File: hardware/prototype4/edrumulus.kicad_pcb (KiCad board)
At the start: 2 copper layers, 67 parts, among them J1 Trigger Connector, J2 Raspberry Pi GPIO pins, U1 ESP32-DEVKIT-V1

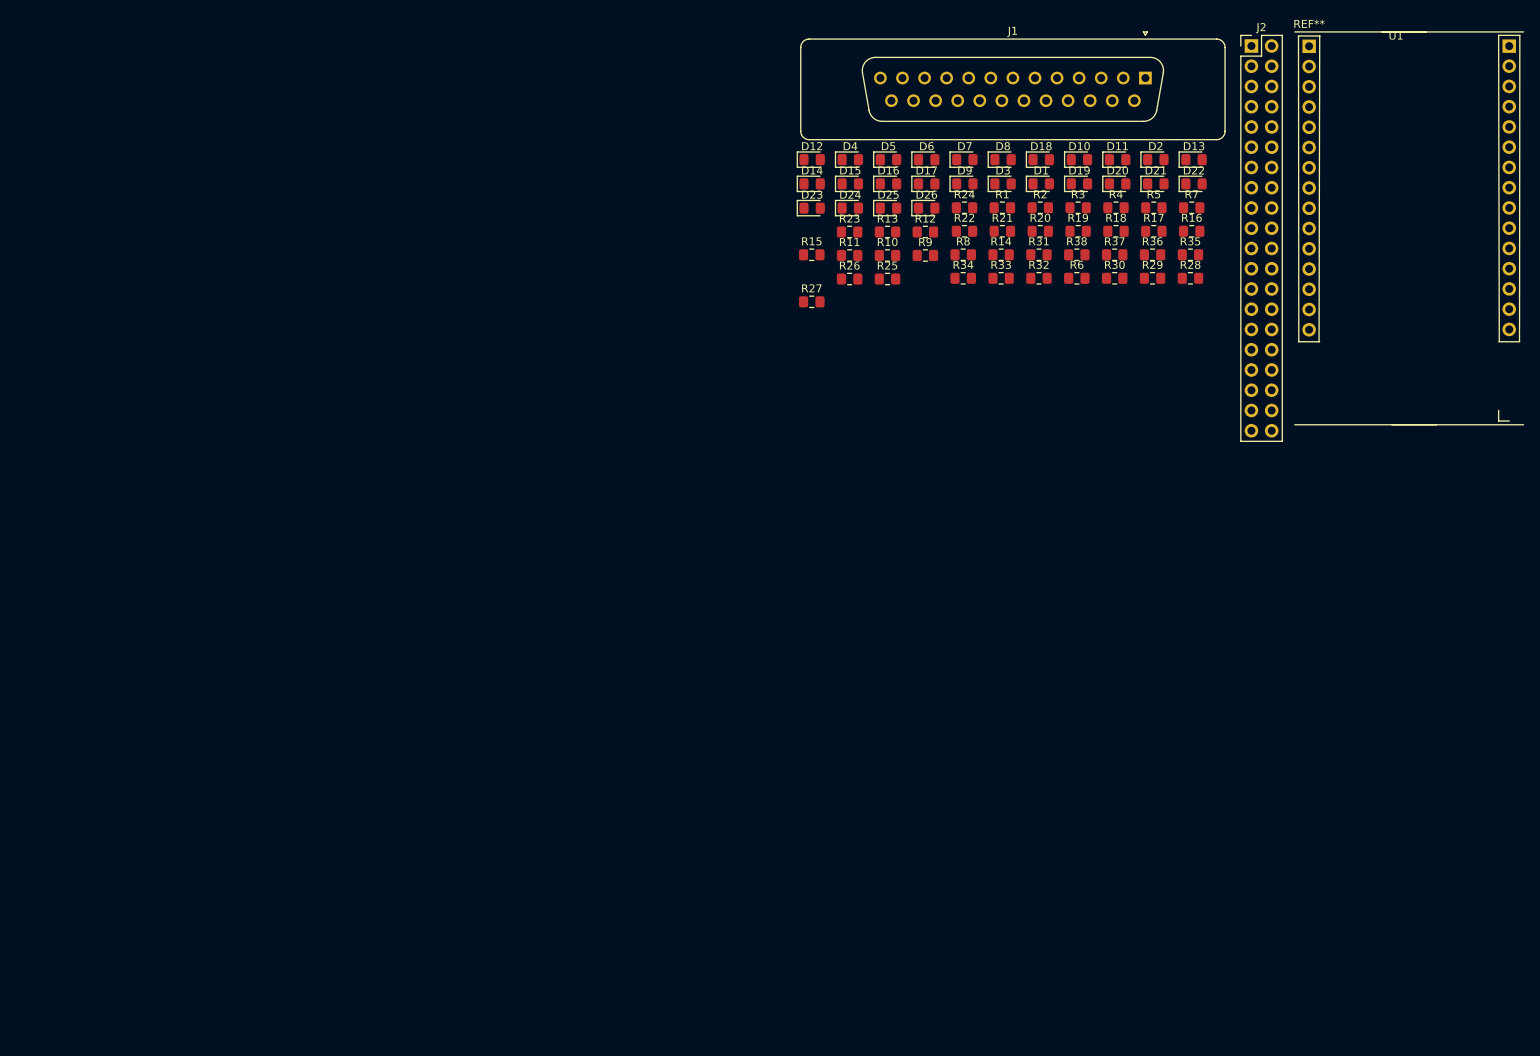
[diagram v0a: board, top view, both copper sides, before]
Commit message: port to KiCad 6
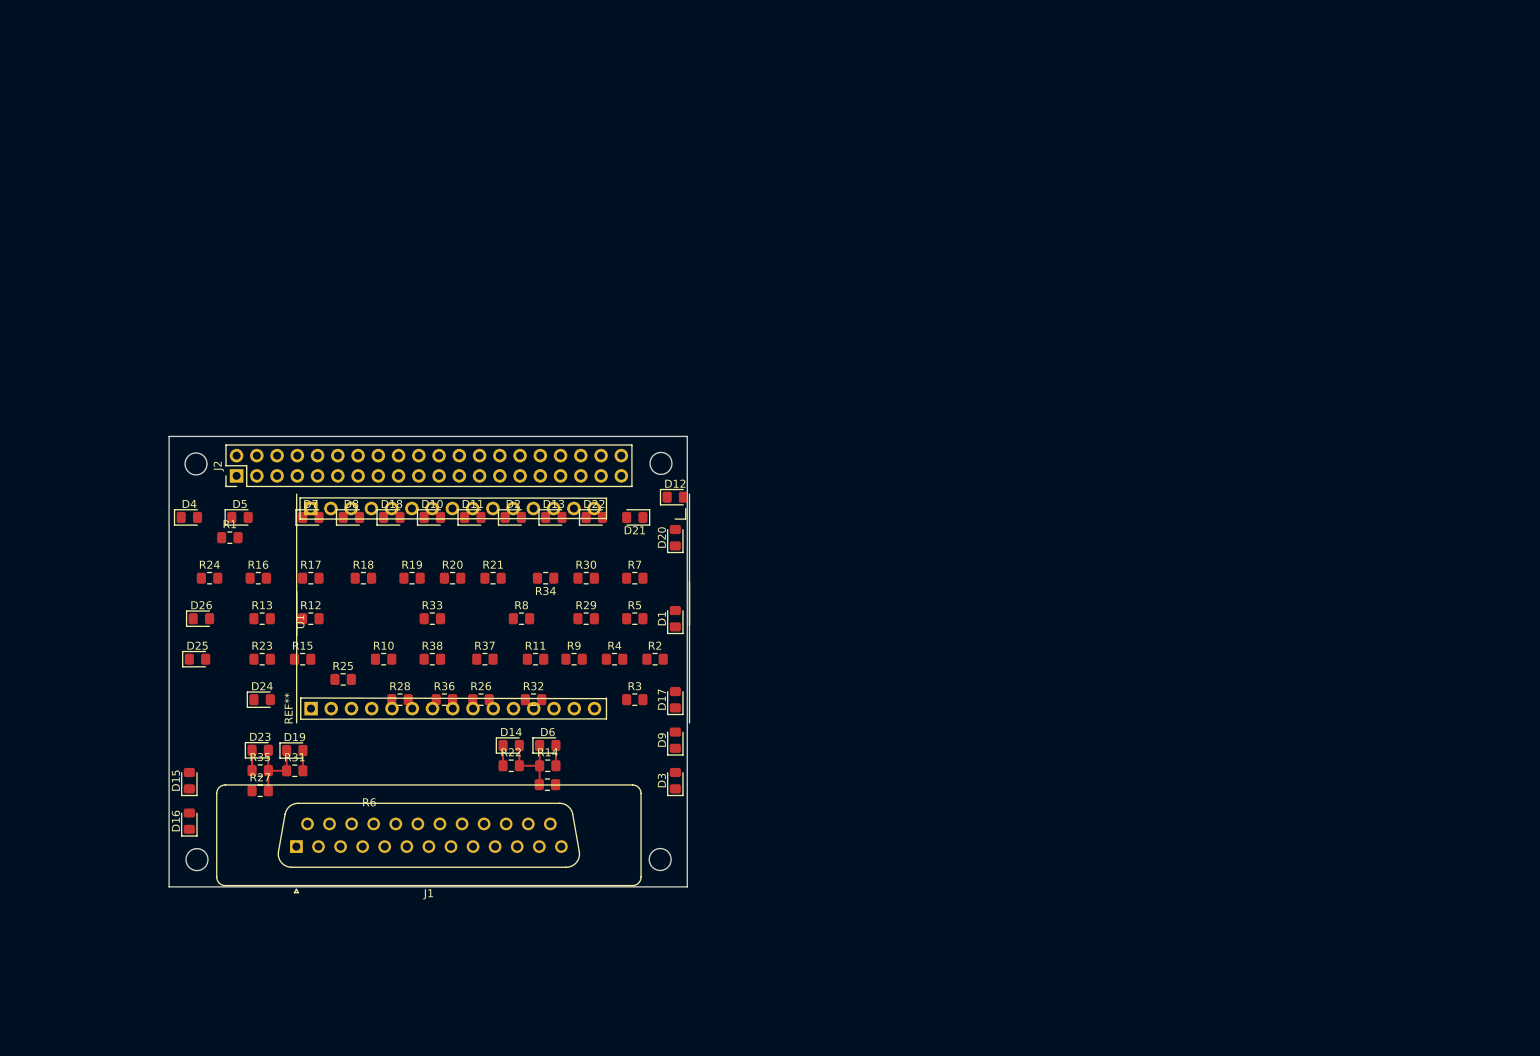
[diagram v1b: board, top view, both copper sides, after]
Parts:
- moved U1 150.3 mm to (124.5, 107.8), turned to 90 degrees
- moved J1 143.6 mm to (122.7, 125.1), turned to 180 degrees
- moved J2 138.2 mm to (115.1, 78.6), turned to 90 degrees
- moved R35 133.4 mm to (118.1, 115.6)
- moved R16 124.9 mm to (117.9, 91.4)
- moved D19 121.4 mm to (122.4, 113.1)
- moved D16 118.7 mm to (109.2, 121.9), turned to 90 degrees
- moved R17 114.3 mm to (124.5, 91.4)
- moved R31 113.6 mm to (122.4, 115.6)
- moved R28 112.4 mm to (135.6, 106.7)
- moved D15 111.7 mm to (109.2, 116.8), turned to 90 degrees
- moved R24 105.5 mm to (111.8, 91.4)
- moved R1 105.4 mm to (114.3, 86.4)
- moved R36 104.9 mm to (141.2, 106.7)
- moved D26 104.5 mm to (110.7, 96.5)
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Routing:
- net GPIO34: track 0.00 -> 10.0 mm
- net GPIO39: track 0.00 -> 9.92 mm
- net CRASH1-SLEEVE: track 0.00 -> 5.08 mm
- net 3V3: track 0.00 -> 5.08 mm
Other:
- board outline added: 65 x 56.5 mm
- net class Default removed

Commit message: component sorting for prototype 4
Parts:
- moved R24 47.5 mm to (152.6, 115.6)
- moved R16 45.5 mm to (156.5, 115.6)
- moved D16 44.3 mm to (152.6, 113.0), turned to 0 degrees
- moved D20 40.3 mm to (139.9, 113.0), turned to 0 degrees
- moved D8 39.7 mm to (156.5, 113.0)
- moved D2 36.9 mm to (127.2, 113.0), turned to 180 degrees
- moved R1 34.3 mm to (127.2, 118.1)
- moved D22 33.1 mm to (144.5, 113.0)
- moved D18 32.3 mm to (148.3, 113.0)
- moved D10 30.5 mm to (131.1, 113.0), turned to 180 degrees
- moved R30 26.4 mm to (148.3, 115.6)
- moved R34 25.9 mm to (144.5, 115.6), turned to 0 degrees
- moved R18 24.1 mm to (131.1, 115.6), turned to 180 degrees
- moved R8 21.7 mm to (152.6, 118.1)
- moved D24 18.6 mm to (135.9, 113.0)
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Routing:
- net GPIO34: track 10.0 -> 0.00 mm
- net GPIO39: track 9.92 -> 0.04 mm
- net CRASH1-SLEEVE: track 5.08 -> 0.00 mm
- net 3V3: track 5.08 -> 0.00 mm

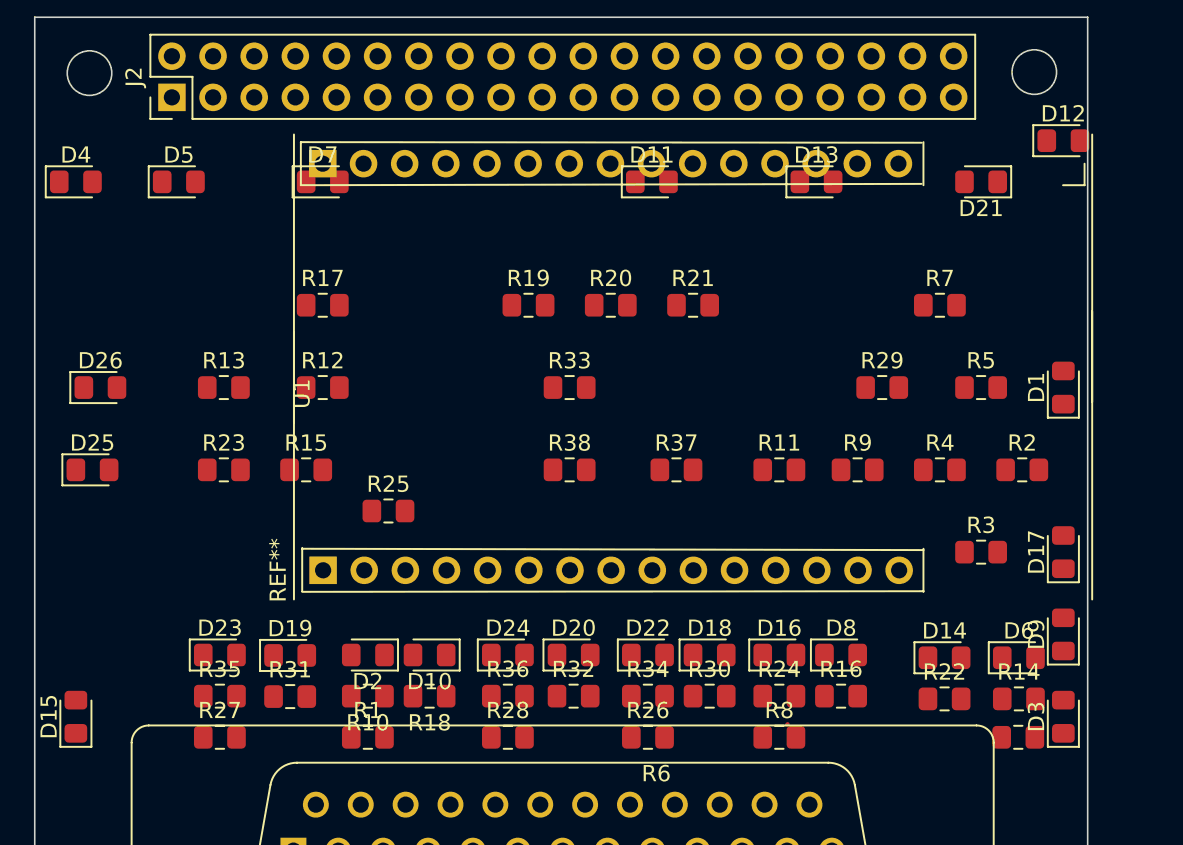
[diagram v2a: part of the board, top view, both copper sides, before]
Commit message: more component sorting for prototype 4
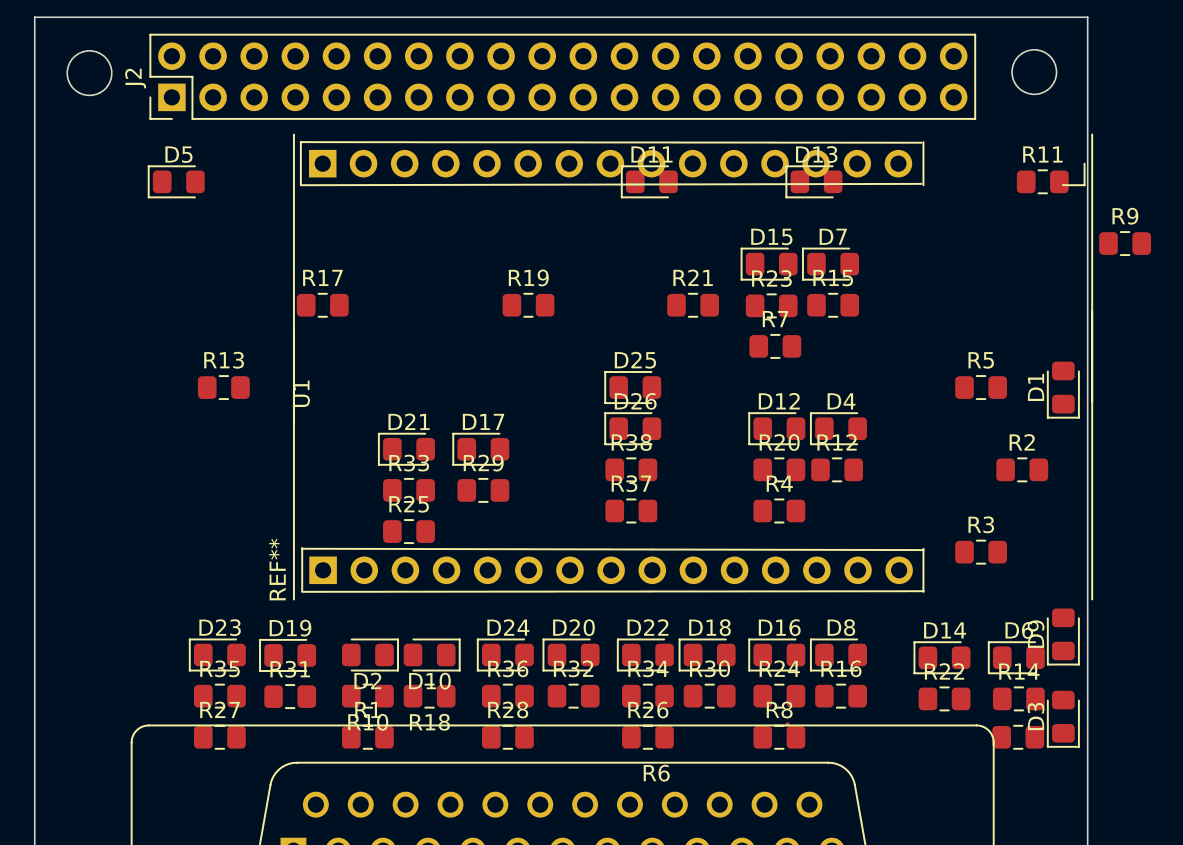
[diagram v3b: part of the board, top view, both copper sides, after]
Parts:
- moved D15 51.2 mm to (152.2, 88.9), turned to 0 degrees
- moved D4 49.6 mm to (156.5, 99.1)
- moved D21 39.0 mm to (129.8, 100.3), turned to 0 degrees
- moved D17 36.4 mm to (134.4, 100.3), turned to 0 degrees
- moved R23 35.3 mm to (152.2, 91.5)
- moved R15 34.1 mm to (156.0, 91.4)
- moved D25 33.9 mm to (143.8, 96.5)
- moved D26 33.1 mm to (143.8, 99.1)
- moved R12 32.2 mm to (156.2, 101.6)
- moved D7 31.9 mm to (156.0, 88.9)
- moved R29 25.4 mm to (134.4, 102.9)
- moved D12 25.0 mm to (152.6, 99.1)
- moved R11 24.1 mm to (168.9, 83.8)
- moved R9 21.6 mm to (174.0, 87.6)
- moved R20 14.5 mm to (152.6, 101.6)
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
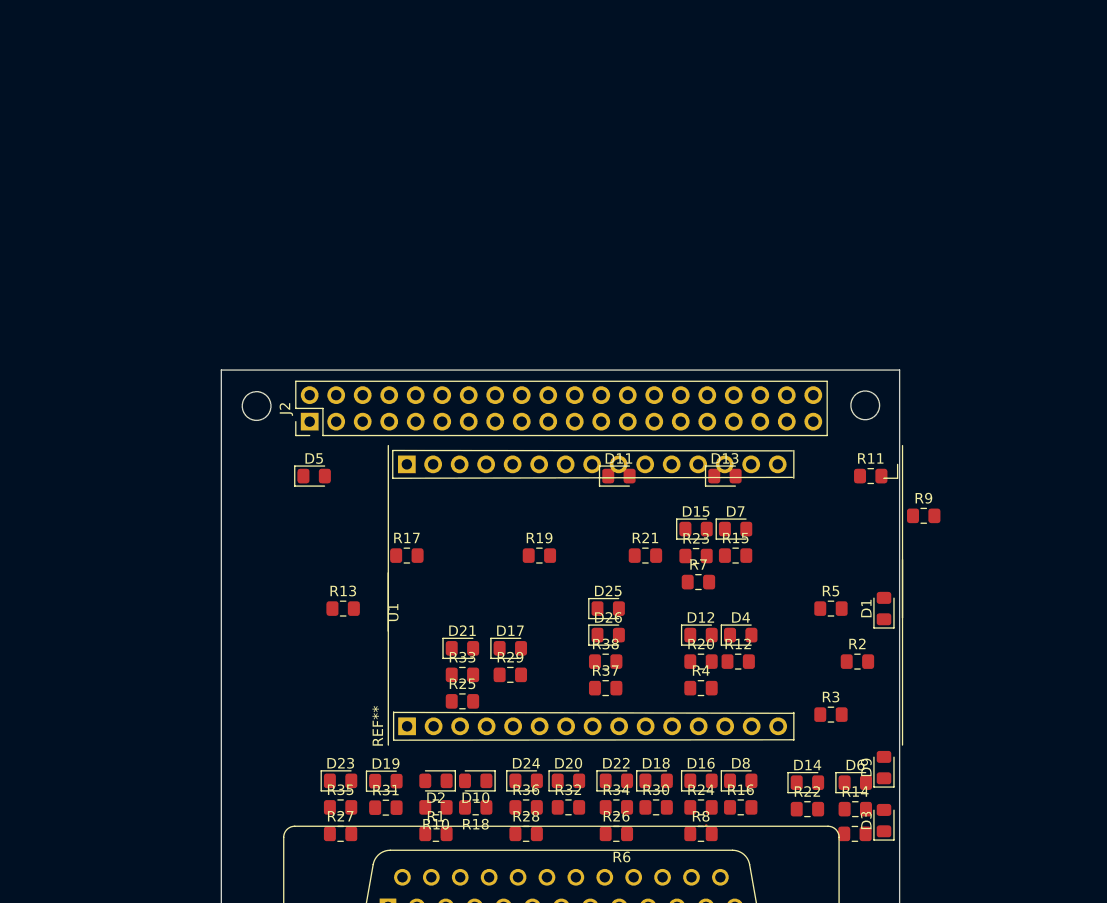
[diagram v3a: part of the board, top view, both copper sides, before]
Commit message: sort more components for prototype 4
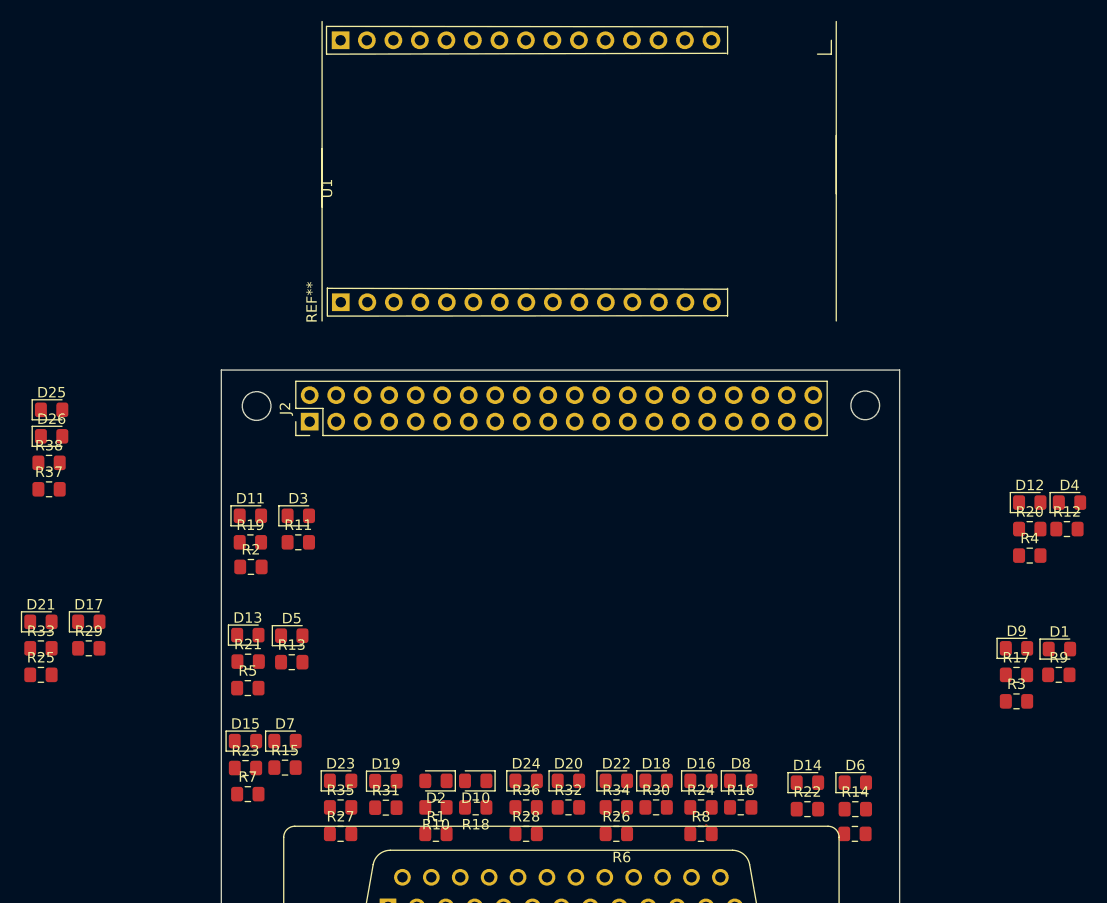
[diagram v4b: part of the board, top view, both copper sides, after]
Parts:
- moved D3 63.3 mm to (114.1, 87.6), turned to 0 degrees
- moved R17 59.5 mm to (182.9, 102.9)
- moved R2 58.8 mm to (109.5, 92.5)
- moved D25 56.6 mm to (90.4, 77.5)
- moved D26 56.6 mm to (90.4, 80.0)
- moved R37 56.6 mm to (90.2, 85.1)
- moved R38 56.6 mm to (90.2, 82.5)
- moved R5 56.4 mm to (109.2, 104.1)
- moved R11 55.2 mm to (114.1, 90.2)
- moved D13 48.2 mm to (109.2, 99.1)
- moved D7 47.7 mm to (112.8, 109.2)
- moved R15 47.7 mm to (112.8, 111.8)
- moved R7 47.7 mm to (109.2, 114.3)
- moved D15 47.7 mm to (109.0, 109.2)
- moved R23 47.7 mm to (109.0, 111.8)
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
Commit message: optimize ESP32 dev board model
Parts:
- moved D15 57.0 mm to (165.1, 99.1)
- moved D7 57.0 mm to (168.9, 99.1)
- moved R15 57.0 mm to (168.9, 101.6)
- moved R23 57.0 mm to (165.1, 101.6)
- moved R7 56.8 mm to (165.1, 104.2)
- moved U1 42.4 mm to (130.2, 107.8)
- moved D19 28.1 mm to (119.9, 141.0)
- moved R1 28.1 mm to (124.7, 146.1)
- moved R14 28.1 mm to (164.9, 143.7)
- moved R22 28.1 mm to (160.3, 143.7)
- moved R26 28.1 mm to (142.0, 146.1)
- moved R27 28.1 mm to (115.6, 146.1)
- moved R28 28.1 mm to (133.3, 146.1)
- moved R31 28.1 mm to (119.9, 143.5)
- moved R6 28.1 mm to (164.9, 146.1)
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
